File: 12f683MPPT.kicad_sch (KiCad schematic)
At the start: 51 parts, among them J1 Conn_01x01_Male, J2 Conn_01x01_Male, J3 Conn_01x01_Male, J4 Conn_01x01_Male, J5 Vin, J6 GND, J7 12V, Q1 BUK9511-55A127, Q2 BUK9511-55A127, Q3 2N2222A, Q4 2N2222A, Q5 2N2907A, SW1 SW_Push, U1 LM7805_TO220, U2 PIC12F683-IP, U3 LM358

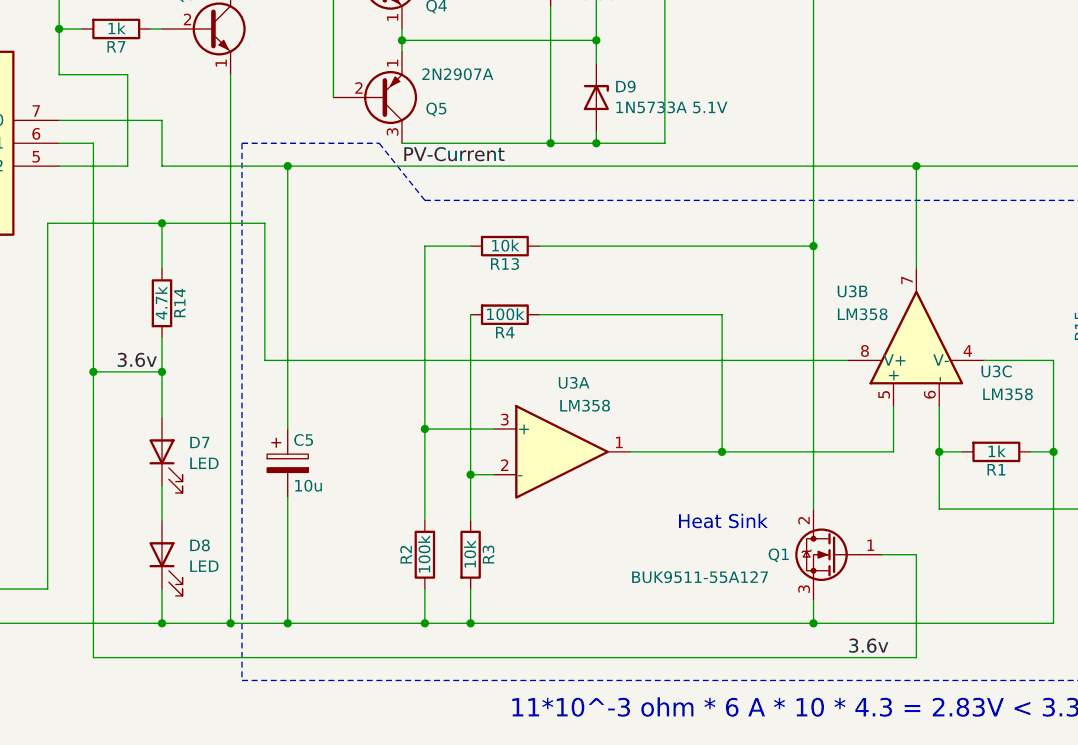
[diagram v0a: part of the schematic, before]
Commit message: Remove C5 capacitor.
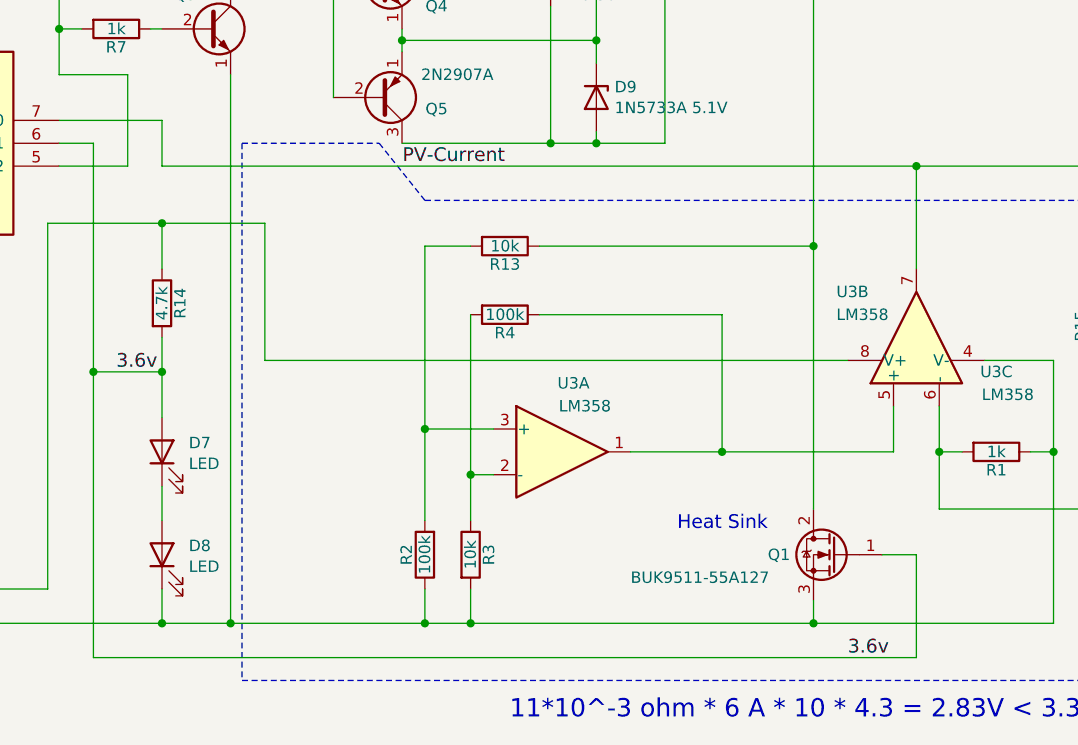
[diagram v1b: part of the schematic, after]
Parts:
- removed C5: 10u, Capacitor_THT:CP_Radial_D8.0mm_P2.50mm, symbol Device:CP
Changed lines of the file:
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@@
 	)
 	(junction
-		(at 154.94 91.44)
-		(diameter 0)
-		(color 0 0 0 0)
-	)
-	(junction
 		(at 54.61 55.88)
 		(diameter 0)
@@
 	)
 	(junction
-		(at 154.94 142.24)
-		(diameter 0)
-		(color 0 0 0 0)
-	)
-	(junction
 		(at 224.79 91.44)
 		(diameter 0)
@@
 	(wire
 		(pts
-			(xy 154.94 91.44) (xy 224.79 91.44)
-		)
-		(stroke
-			(width 0)
-			(type default)
-		)
-	)
-	(wire
-		(pts
 			(xy 129.54 88.9) (xy 133.35 88.9)
 		)
@@
 	(wire
 		(pts
-			(xy 154.94 91.44) (xy 140.97 91.44)
+			(xy 140.97 91.44) (xy 224.79 91.44)
 		)
 		(stroke
@@
 	(wire
 		(pts
-			(xy 154.94 128.27) (xy 154.94 142.24)
-		)
-		(stroke
-			(width 0)
-			(type default)
-		)
-	)
-	(wire
-		(pts
 			(xy 224.79 146.05) (xy 224.79 134.62)
 		)
@@
 	(wire
 		(pts
-			(xy 154.94 142.24) (xy 148.59 142.24)
-		)
-		(stroke
-			(width 0)
-			(type default)
-		)
-	)
-	(wire
-		(pts
-			(xy 170.18 142.24) (xy 154.94 142.24)
+			(xy 148.59 142.24) (xy 170.18 142.24)
 		)
 		(stroke
@@
 	(wire
 		(pts
-			(xy 154.94 120.65) (xy 154.94 91.44)
-		)
-		(stroke
-			(width 0)
-			(type default)
-		)
-	)
-	(wire
-		(pts
 			(xy 83.82 55.88) (xy 82.55 55.88)
 		)
@@
 					(unit 1)
 				)
-			)
-		)
-	)
-	(symbol
-		(lib_id "Device:CP")
-		(at 154.94 124.46 0)
-		(unit 1)
-		(exclude_from_sim no)
-		(in_bom yes)
-		(on_board yes)
-		(dnp no)
-		(property "Reference" "C5"
-			(at 155.575 121.92 0)
-			(effects
-				(font
-					(size 1.27 1.27)
-				)
-				(justify left)
-			)
-		)
-		(property "Value" "10u"
-			(at 155.575 127 0)
-			(effects
-				(font
-					(size 1.27 1.27)
-				)
-				(justify left)
-			)
-		)
-		(property "Footprint" "Capacitor_THT:CP_Radial_D8.0mm_P2.50mm"
-			(at 155.9052 128.27 0)
-			(effects
-				(font
-					(size 0.762 0.762)
-				)
-				(hide yes)
-			)
-		)
-		(property "Datasheet" ""
-			(at 154.94 124.46 0)
-			(effects
-				(font
-					(size 1.524 1.524)
-				)
-			)
-		)
-		(property "Description" ""
-			(at 154.94 124.46 0)
-			(effects
-				(font
-					(size 1.27 1.27)
-				)
-			)
-		)
-		(pin "1"
-		)
-		(pin "2"
-		)
-		(instances
-			(project ""
-				(path "/c54864ce-ba59-4422-a8c7-824cf583dfc9"
-					(reference "C5")
-					(unit 1)
-				)

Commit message: Revert "Remove C5 capacitor."
This reverts commit 91564baa6f44f8037db3e26806d1f3bf7336a2bb.
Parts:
- added C5: 10u, Capacitor_THT:CP_Radial_D8.0mm_P2.50mm, symbol Device:CP
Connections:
- net GNDPWR: now also C5.2
- net PV-Current: now also C5.1
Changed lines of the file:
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@@
 	)
 	(junction
+		(at 154.94 91.44)
+		(diameter 0)
+		(color 0 0 0 0)
+	)
+	(junction
 		(at 54.61 55.88)
 		(diameter 0)
@@
 	)
 	(junction
+		(at 154.94 142.24)
+		(diameter 0)
+		(color 0 0 0 0)
+	)
+	(junction
 		(at 224.79 91.44)
 		(diameter 0)
@@
 	(wire
 		(pts
+			(xy 154.94 91.44) (xy 224.79 91.44)
+		)
+		(stroke
+			(width 0)
+			(type default)
+		)
+	)
+	(wire
+		(pts
 			(xy 129.54 88.9) (xy 133.35 88.9)
 		)
@@
 	(wire
 		(pts
-			(xy 140.97 91.44) (xy 224.79 91.44)
+			(xy 154.94 91.44) (xy 140.97 91.44)
 		)
 		(stroke
@@
 	(wire
 		(pts
+			(xy 154.94 128.27) (xy 154.94 142.24)
+		)
+		(stroke
+			(width 0)
+			(type default)
+		)
+	)
+	(wire
+		(pts
 			(xy 224.79 146.05) (xy 224.79 134.62)
 		)
@@
 	(wire
 		(pts
-			(xy 148.59 142.24) (xy 170.18 142.24)
+			(xy 154.94 142.24) (xy 148.59 142.24)
+		)
+		(stroke
+			(width 0)
+			(type default)
+		)
+	)
+	(wire
+		(pts
+			(xy 170.18 142.24) (xy 154.94 142.24)
 		)
 		(stroke
@@
 	(wire
 		(pts
+			(xy 154.94 120.65) (xy 154.94 91.44)
+		)
+		(stroke
+			(width 0)
+			(type default)
+		)
+	)
+	(wire
+		(pts
 			(xy 83.82 55.88) (xy 82.55 55.88)
 		)
@@
 					(unit 1)
 				)
+			)
+		)
+	)
+	(symbol
+		(lib_id "Device:CP")
+		(at 154.94 124.46 0)
+		(unit 1)
+		(exclude_from_sim no)
+		(in_bom yes)
+		(on_board yes)
+		(dnp no)
+		(property "Reference" "C5"
+			(at 155.575 121.92 0)
+			(effects
+				(font
+					(size 1.27 1.27)
+				)
+				(justify left)
+			)
+		)
+		(property "Value" "10u"
+			(at 155.575 127 0)
+			(effects
+				(font
+					(size 1.27 1.27)
+				)
+				(justify left)
+			)
+		)
+		(property "Footprint" "Capacitor_THT:CP_Radial_D8.0mm_P2.50mm"
+			(at 155.9052 128.27 0)
+			(effects
+				(font
+					(size 0.762 0.762)
+				)
+				(hide yes)
+			)
+		)
+		(property "Datasheet" ""
+			(at 154.94 124.46 0)
+			(effects
+				(font
+					(size 1.524 1.524)
+				)
+			)
+		)
+		(property "Description" ""
+			(at 154.94 124.46 0)
+			(effects
+				(font
+					(size 1.27 1.27)
+				)
+			)
+		)
+		(pin "1"
+		)
+		(pin "2"
+		)
+		(instances
+			(project ""
+				(path "/c54864ce-ba59-4422-a8c7-824cf583dfc9"
+					(reference "C5")
+					(unit 1)
+				)
